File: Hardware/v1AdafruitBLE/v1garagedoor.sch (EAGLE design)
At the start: 27 parts, among them IC1 78V, Q1 2N3904, U1 ATMEGA328P_PDIP, X1 16mhz

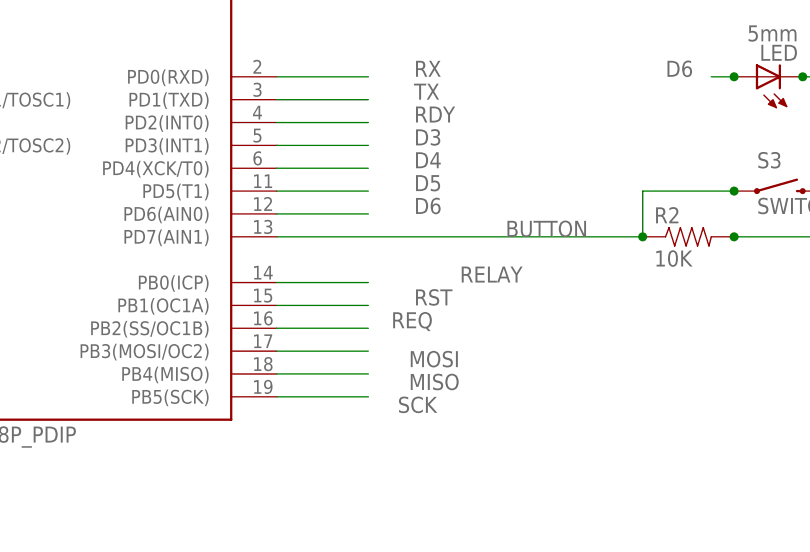
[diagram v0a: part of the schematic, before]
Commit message: added some documentation made some changes to the board layout because of the v1 board has some needed changes. I expect there to be a few more changes, around the silkscreen output
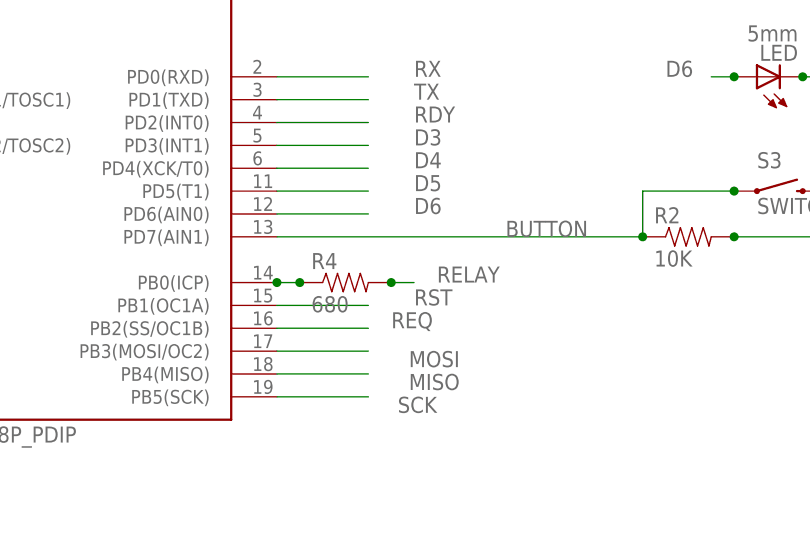
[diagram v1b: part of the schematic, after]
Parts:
- added R4: 680, SparkFun-Resistors:RESISTORAXIAL-0.3
- C1, C2: MOUSER (none) -> 594-S200K25SL0N63L6R
- C3, C4, C6, C7: MOUSER (none) -> 810-FK18X5R1A334K
- D1, D2: MOUSER (none) -> 621-1N4004
- IC1: MOUSER (none) -> 863-MC7805CTG
- JP1: MOUSER (none) -> 571-5-146252-3
- JP2: MOUSER (none) -> 992-10FX1-254MM
- Q1: MOUSER (none) -> 610-2N3904
- R1, R2: MOUSER (none) -> 603-CFR-25JR-5210K
- R3: MOUSER (none) -> 603-CFR-25JR-52220R
- RELAY: MOUSER (none) -> 655-ORWH-SH105D1F000
- S3, S4: MOUSER (none) -> 693-1301.9301
- U$1: MOUSER (none) -> 992-CON-SOCJ-2155
- U1: MOUSER (none) -> 556-ATMEGA328P-PU
- X1: MOUSER (none) -> 520-160-20-46X
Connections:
- new net N$7: R4.1, U1.PB0(ICP)
- net RELAY: now also R4.2; no longer U1.PB0(ICP)

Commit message: just updating the repo
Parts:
- C1, C2: value 20pF -> 33pF
- C6, C7: value .33uF -> .1uF
- JP4: value test point relay -> (none)
- R4: value 680 -> 2K4
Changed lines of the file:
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@@
 <attribute name="MOUSER" value="520-160-20-46X"/>
 </part>
-<part name="C1" library="SparkFun-Capacitors" deviceset="CAP" device="PTH1" value="20pF">
+<part name="C1" library="SparkFun-Capacitors" deviceset="CAP" device="PTH1" value="33pF">
 <attribute name="MOUSER" value="594-S200K25SL0N63L6R"/>
 </part>
-<part name="C2" library="SparkFun-Capacitors" deviceset="CAP" device="PTH1" value="20pF">
+<part name="C2" library="SparkFun-Capacitors" deviceset="CAP" device="PTH1" value="33pF">
 <attribute name="MOUSER" value="594-S200K25SL0N63L6R"/>
 </part>
@@
 <attribute name="MOUSER" value="810-FK18X5R1A334K"/>
 </part>
-<part name="C6" library="SparkFun-Capacitors" deviceset="CAP" device="KIT" value=".33uF">
+<part name="C6" library="SparkFun-Capacitors" deviceset="CAP" device="KIT" value=".1uF">
 <attribute name="MOUSER" value="810-FK18X5R1A334K"/>
 </part>
-<part name="C7" library="SparkFun-Capacitors" deviceset="CAP" device="KIT" value=".33uF">
+<part name="C7" library="SparkFun-Capacitors" deviceset="CAP" device="KIT" value=".1uF">
 <attribute name="MOUSER" value="810-FK18X5R1A334K"/>
 </part>
@@
 <part name="SUPPLY6" library="SparkFun-Aesthetics" deviceset="5V" device=""/>
 <part name="SUPPLY7" library="SparkFun-Aesthetics" deviceset="5V" device=""/>
-<part name="JP4" library="SparkFun-Connectors" deviceset="M03" device="LOCK" value="test point relay"/>
+<part name="JP4" library="SparkFun-Connectors" deviceset="M03" device="LOCK"/>
 <part name="S3" library="SparkFun-Electromechanical" deviceset="SWITCH-MOMENTARY-2" device="PTH">
 <attribute name="MOUSER" value="693-1301.9301"/>
@@
 <attribute name="MOUSER" value="655-ORWH-SH105D1F000"/>
 </part>
-<part name="R4" library="SparkFun-Resistors" deviceset="RESISTOR" device="AXIAL-0.3" value="680">
+<part name="R4" library="SparkFun-Resistors" deviceset="RESISTOR" device="AXIAL-0.3" value="2K4">
 <attribute name="MOUSER" value="603-CFR-25JR-52-680R"/>
 </part>
